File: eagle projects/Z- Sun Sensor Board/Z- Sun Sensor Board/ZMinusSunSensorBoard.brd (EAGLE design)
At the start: 91 x 91 mm, 49 parts, among them U2 ADS7841E_2K5, U4 LM20BIM7X_NOPB, U6 TLV9051IDCKR, U8 TLV9051IDCKR, U9 TLV9051IDCKR

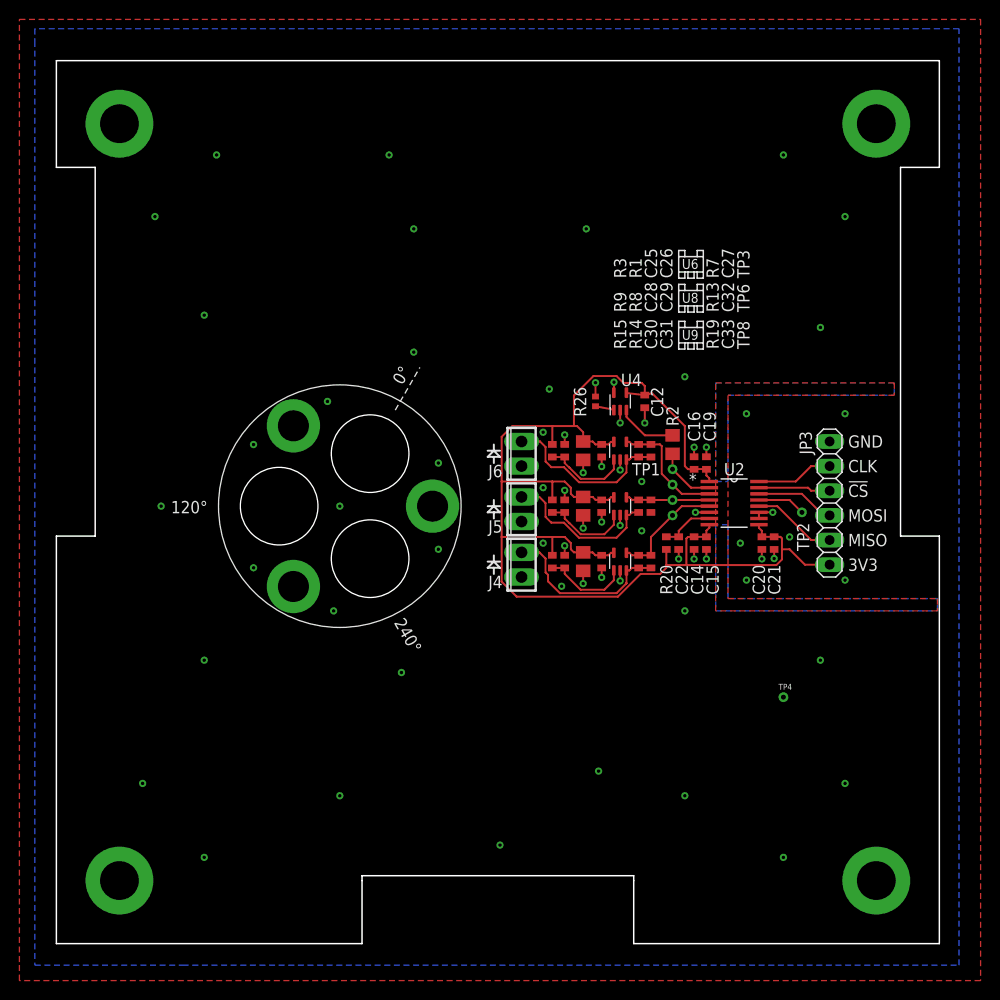
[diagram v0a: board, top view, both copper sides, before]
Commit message: Added X & Y sun sensor connectors to Z- Sun Sense Board
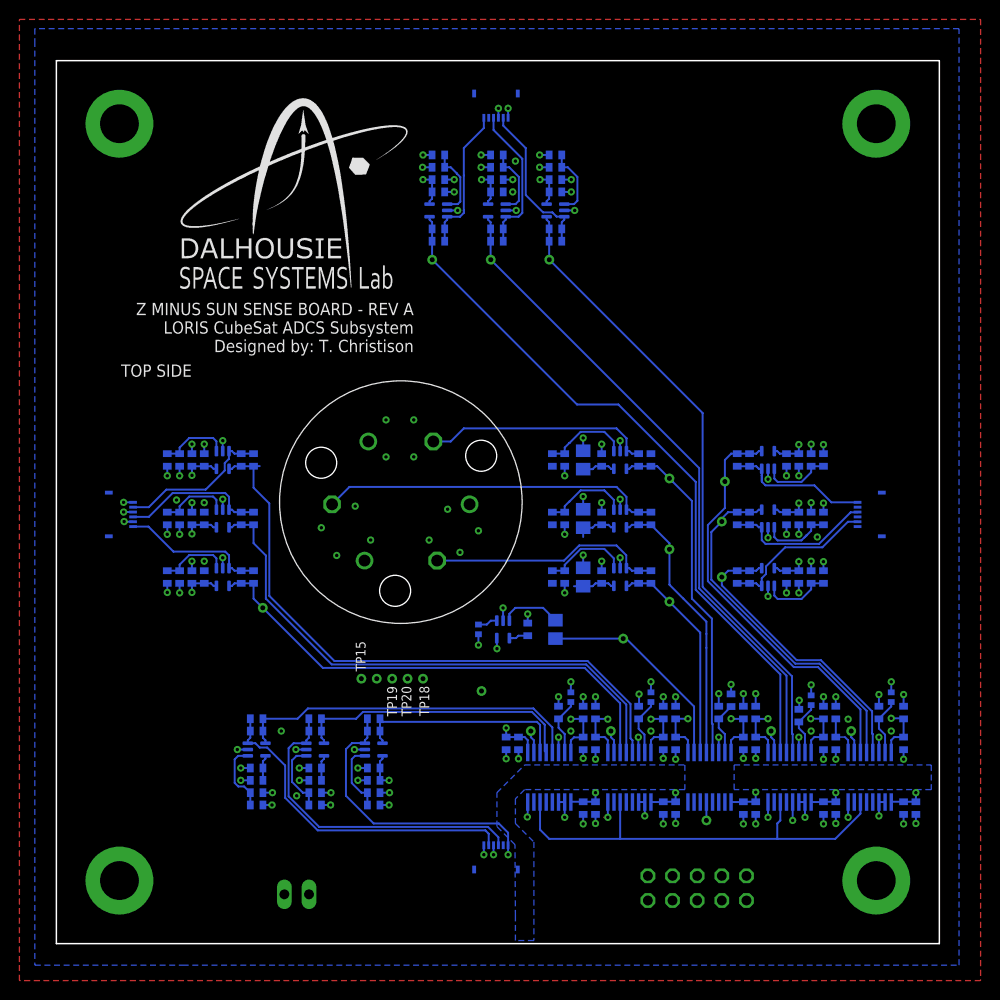
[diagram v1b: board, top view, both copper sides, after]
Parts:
- removed J6: (no value), my_library:2POL254
- added C1, C45, C47, C50, C66, C72, C74, C77, C80, C89, C91, C94: 1u, resistor:C0402
- added C100, C101, C105, C110, C111, C115, C116, C54, C70, C71, C84, C98: 0.022u, resistor:C0402
- added C102, C104, C107, C109, C112, C114, C46, C48, C49, C51, C53, C65, C67, C69, C73, C75, C76, C78, C79, C81, C83, C86, C88, C90, C92, C93, C95, C97: 0.1u, resistor:C0402
- added C103, C106, C108, C113, C52, C55, C68, C82, C85, C87, C96, C99: 4.7u, resistor:C0402
- added J2, J3: HIROSE_FH19C-6S-0.5SH(10), my_library:HIROSE_FH19C-6S-0.5SH(10)
- added JP1: (no value), pinhead:1X02
- added R10, R4, R5, R6: 10k, rcl:R0402
- added R22, R25, R32, R38, R44, R50, R53, R56, R59, R62, R65, R68: 280R, resistor:R0402
- added R23, R28, R33, R39, R45, R51, R54, R57, R60, R63, R66, R69: 13.7k, resistor:R0402
- added R24, R31, R34, R40, R46, R52, R55, R58, R61, R64, R67, R70: 3.74k, resistor:R0402
- added TP10, TP11, TP12, TP13, TP14, TP15, TP16, TP17, TP18, TP19, TP20, TP21, TP22, TP5, TP7, TP9: TESTPOINT, my_library:TP_P76H50
- added U1, U13, U25, U27: ADS7841E_2K5, my_library:DBQ16
- added U15, U19, U21, U23, U24, U26, U28, U29, U3, U30, U31, U32: TLV9051IDCKR, my_library:SC70-5P65_210X110L36X22N_TLV9051
- A1: value SUN_SENSOR_MOUNT -> XY_SUN_SENSOR; device my_library:SUN_SENOR_MASK -> my_library:XY_SUN_SENOR_MASK
- J4, J5: value (none) -> HIROSE_FH19C-6S-0.5SH(10); device my_library:2POL254 -> my_library:HIROSE_FH19C-6S-0.5SH(10)
- JP3: device pinhead:1X06 -> pinhead:2X05
- moved JP3 42.0 mm to (66.0, 5.71), flipped to the bottom, turned to 0 degrees
- moved J5 41.7 mm to (45.3, 86.4), flipped to the bottom, turned to 180 degrees
- moved TP2 33.2 mm to (67.0, 12.7), flipped to the bottom, turned to 90 degrees
- moved TP4 31.1 mm to (43.8, 26.0), flipped to the bottom
- moved J4 30.3 mm to (45.3, 8.89), flipped to the bottom, turned to 0 degrees
- moved C19 29.1 mm to (63.8, 20.6), flipped to the bottom, turned to 270 degrees
- moved U2 28.4 mm to (67.3, 17.1), flipped to the bottom, turned to 270 degrees
- moved C20 27.4 mm to (70.8, 14.0), flipped to the bottom
- moved C21 27.4 mm to (72.1, 14.0), flipped to the bottom
- moved C12 26.4 mm to (48.6, 32.4), flipped to the bottom, turned to 90 degrees
- moved R26 26.4 mm to (43.5, 32.4), flipped to the bottom, turned to 270 degrees
- moved U4 26.4 mm to (46.0, 32.4), flipped to the bottom, turned to 180 degrees
- moved C16 25.8 mm to (63.8, 23.8), flipped to the bottom
- moved R2 22.5 mm to (51.4, 32.4), flipped to the bottom
- moved C15 21.0 mm to (70.8, 20.6), flipped to the bottom
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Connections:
- new net !CS!_SUN_X+: JP3.2, U25.15
- new net !CS!_SUN_X-: JP3.7, U13.15
- new net !CS!_SUN_Y+: JP3.4, U27.15
- new net !CS!_SUN_Y-: JP3.9, U1.15
- new net !CS!_SUN_Z-: JP3.6
- new net N$10: TP13.1, U13.2
- new net N$11: TP21.1, U27.2
- new net N$14: TP22.1, U1.2
- new net N$22: C51.1, R5.1, U13.7
- new net N$23: C100.1, J5.3, R31.1, U23.3
- new net N$24: C81.1, R10.1, U1.7
- new net N$25: C95.1, R6.1, U27.7
- new net N$29: C84.1, J5.1, R24.1, U3.3
- new net N$31: R22.2, R23.1, U3.1
- new net N$34: R25.2, R28.1, U23.1
- new net N$35: C101.1, J5.5, R34.1, U24.3
- new net N$36: R32.2, R33.1, U24.1
- new net N$37: C98.1, J4.1, R64.1, U30.3
- new net N$38: C54.1, J3.1, R40.1, U15.3
- new net N$4: C102.1, R4.1, U25.7
- new net N$41: R38.2, R39.1, U15.1
- new net N$44: C70.1, J3.3, R46.1, U19.3
- new net N$45: R44.2, R45.1, U19.1
- new net N$46: C71.1, J3.5, R52.1, U21.3
- new net N$47: R50.2, R51.1, U21.1
- new net N$49: C105.1, J2.1, R55.1, U26.3
- new net N$5: TP17.1, U25.2
- new net N$54: R53.2, R54.1, U26.1
- new net N$55: C110.1, J2.3, R58.1, U28.3
- new net N$56: R56.2, R57.1, U28.1
- new net N$57: C111.1, J2.5, R61.1, U29.3
- new net N$58: R59.2, R60.1, U29.1
- new net N$61: R62.2, R63.1, U30.1
- new net N$63: C115.1, J4.3, R67.1, U31.3
- new net N$64: R65.2, R66.1, U31.1
- new net N$65: C116.1, J4.5, R70.1, U32.3
- new net N$66: R68.2, R69.1, U32.1
- new net N$67: JP3.8
- new net N$68: JP3.10
- new net X+_0_DEGREES: C105.2, R55.2, TP14.1, U25.3, U26.4
- new net X+_120_DEGREES: C110.2, R58.2, TP15.1, U25.4, U28.4
- new net X+_240_DEGREES: C111.2, R61.2, TP16.1, U25.5, U29.4
- new net X-_0_DEGREES: C54.2, R40.2, TP10.1, U13.3, U15.4
- new net X-_120_DEGREES: C70.2, R46.2, TP11.1, U13.4, U19.4
- new net X-_240_DEGREES: C71.2, R52.2, TP12.1, U13.5, U21.4
- new net Y+_0_DEGREES: C98.2, R64.2, TP18.1, U27.3, U30.4
- new net Y+_120_DEGREES: C115.2, R67.2, TP19.1, U27.4, U31.4
- new net Y+_240_DEGREES: C116.2, R70.2, TP20.1, U27.5, U32.4
- new net Y-_0_DEGREES: C84.2, R24.2, TP5.1, U1.3, U3.4
- new net Y-_120_DEGREES: C100.2, R31.2, TP7.1, U1.4, U23.4
- new net Y-_240_DEGREES: C101.2, R34.2, TP9.1, U1.5, U24.4
- net !CS!_SUN_Z+: no longer JP3.3
- net +3V3: now also C1.1, C103.1, C104.1, C106.1, C107.1, C108.1, C109.1, C112.1, C113.1, C114.1, C45.1, C46.1, C47.1, C48.1, C49.1, C50.1, C52.1, C53.1, C55.1, C65.1, C66.1, C67.1, C68.1, C69.1, C72.1, C73.1, C74.1, C75.1, C76.1, C77.1, C78.1, C79.1, C80.1, C82.1, C83.1, C85.1, C86.1, C87.1, C88.1, C89.1, C90.1, C91.1, C92.1, C93.1, C94.1, C96.1, C97.1, C99.1, JP1.1, R10.2, R23.2, R28.2, R33.2, R39.2, R4.2, R45.2, R5.2, R51.2, R54.2, R57.2, R6.2, R60.2, R63.2, R66.2, R69.2, U1.1, U1.8, U1.9, U13.1, U13.8, U13.9, U15.5, U19.5, U21.5, U23.5, U24.5, U25.1, U25.8, U25.9, U26.5, U27.1, U27.8, U27.9, U28.5, U29.5, U3.5, U30.5, U31.5, U32.5; no longer JP3.6
- net 0_DEGREES: now also U2.4; no longer U2.3
- net 120_DEGREES: now also U2.5; no longer U2.4
- net 240_DEGREES: now also U2.3; no longer U2.5
- net GND: now also A1.A1, A1.A2, A1.A3, C1.2, C102.2, C103.2, C104.2, C106.2, C107.2, C108.2, C109.2, C112.2, C113.2, C114.2, C45.2, C46.2, C47.2, C48.2, C49.2, C50.2, C51.2, C52.2, C53.2, C55.2, C65.2, C66.2, C67.2, C68.2, C69.2, C72.2, C73.2, C74.2, C75.2, C76.2, C77.2, C78.2, C79.2, C80.2, C81.2, C82.2, C83.2, C85.2, C86.2, C87.2, C88.2, C89.2, C90.2, C91.2, C92.2, C93.2, C94.2, C95.2, C96.2, C97.2, C99.2, J2.2, J2.4, J2.6, J2.7, J2.8, J3.2, J3.4, J3.6, J3.7, J3.8, J4.2, J4.4, J4.6, J4.7, J4.8, J5.2, J5.4, J5.6, J5.7, J5.8, JP1.2, R22.1, R25.1, R32.1, R38.1, R44.1, R50.1, R53.1, R56.1, R59.1, R62.1, R65.1, R68.1, U1.10, U1.11, U1.6, U13.10, U13.11, U13.6, U15.2, U19.2, U21.2, U23.2, U24.2, U25.10, U25.11, U25.6, U26.2, U27.10, U27.11, U27.6, U28.2, U29.2, U3.2, U30.2, U31.2, U32.2; no longer J4.1, J5.1, J6.1, JP3.1
- net N$12: now also A1.C3; no longer J4.2
- net N$3: now also A1.C1; no longer J6.2
- net N$8: now also A1.C2; no longer J5.2
- net UCB0_SPI_CLK: now also JP3.5, U1.16, U13.16, U25.16, U27.16; no longer JP3.2
- net UCB0_SPI_MISO: now also JP3.1, U1.12, U13.12, U25.12, U27.12; no longer JP3.5
- net UCB0_SPI_MOSI: now also JP3.3, U1.14, U13.14, U25.14, U27.14; no longer JP3.4
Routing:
- net GND: track 28.8 -> 121.4 mm, vias 69 -> 120
- net Y-_0_DEGREES: track 0.00 -> 72.7 mm
- net Y-_120_DEGREES: track 0.00 -> 68.0 mm
- net Y-_240_DEGREES: track 0.00 -> 65.7 mm
- net X+_240_DEGREES: track 0.00 -> 64.2 mm
- net X+_120_DEGREES: track 0.00 -> 57.4 mm
- net X+_0_DEGREES: track 0.00 -> 51.5 mm
- net X-_0_DEGREES: track 0.00 -> 43.4 mm
- net UCB0_SPI_MOSI: track 7.58 -> 46.3 mm
- net X-_120_DEGREES: track 0.00 -> 37.1 mm
- net Y+_240_DEGREES: track 0.00 -> 36.3 mm
- net N$65: track 0.00 -> 34.5 mm
- net N$63: track 0.00 -> 33.8 mm
- net X-_240_DEGREES: track 0.00 -> 30.6 mm
- net N$37: track 0.00 -> 30.2 mm, vias 0 -> 1
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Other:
- outline, holes or cut-outs redrawn
- board text added: "+3V3"
- board text added: "BOTTOM SIDE"
- board text added: "C72"
- board text added: "C90"
- board text added: "Designed by: T. Christison"
- board text added: "LORIS CubeSat ADCS Subsystem"
- board text added: "TOP SIDE"
- board text added: "U15"
- board text added: "U19"
- board text added: "U21"
- board text added: "U23"
- board text added: "U24"
- board text added: "U26"
- board text added: "U28"
- board text added: "U29"
- board text added: "U30"
- board text added: "U31"
- board text added: "U32"
- board text added: "Z MINUS SUN SENSE BOARD - REV A"
- board text removed: "!CS"
- board text removed: "3V3"
- board text removed: "CLK"
- board text removed: "Dalhousie Space Systems Lab"
- board text removed: "Designed by T. Christison"
- board text removed: "MISO"
- board text removed: "MOSI"
- board text removed: "Z- SUN SENSOR BOARD - Rev A"

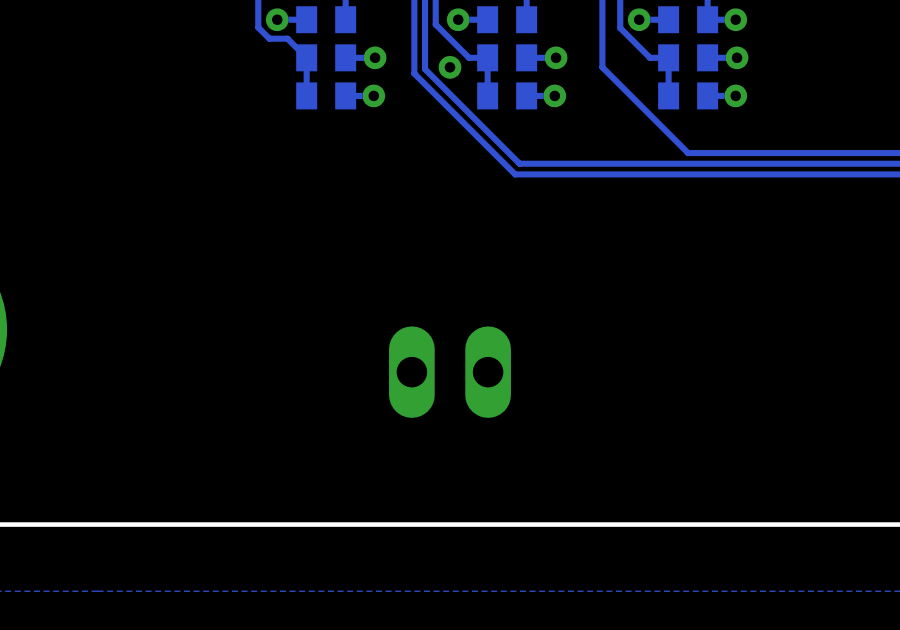
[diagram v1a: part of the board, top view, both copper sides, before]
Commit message: Added indicator LED
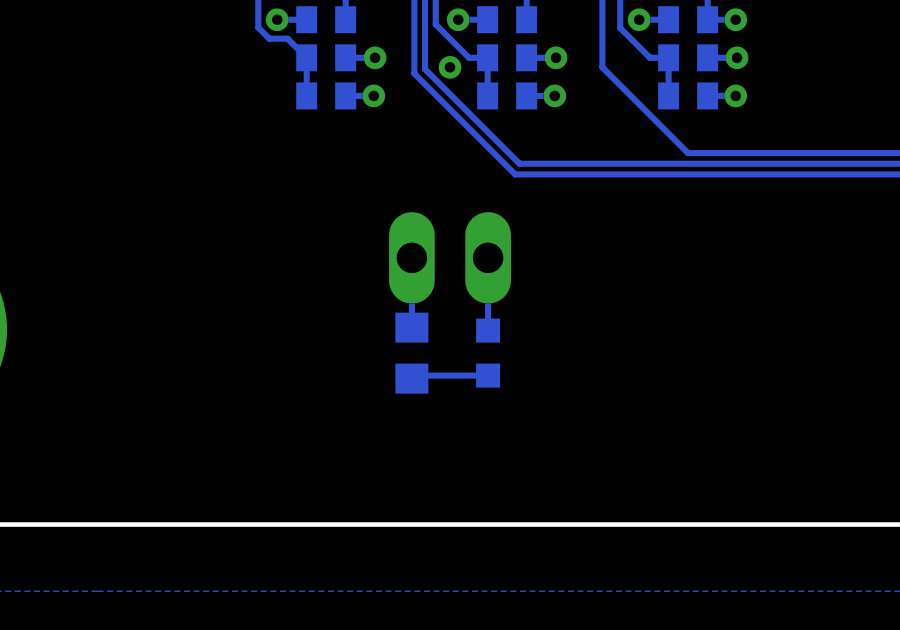
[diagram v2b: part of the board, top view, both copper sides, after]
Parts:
- added LED1: (no value), led:CHIP-LED0603
- added R11: (no value), rcl:R0603
- moved JP1 3.81 mm to (24.8, 8.89)
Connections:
- new net N$48: LED1.A, R11.1
- net +3V3: now also R11.2
- net GND: now also LED1.C
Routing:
- net N$48: track 0.00 -> 2.58 mm
- net GND: track 121.4 -> 123.8 mm
- net +3V3: track 147.4 -> 149.7 mm
